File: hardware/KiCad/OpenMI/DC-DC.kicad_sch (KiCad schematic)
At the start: 37 parts, among them Q4 GAN7R0-150LBEZ, Q5 GAN7R0-150LBEZ, U3 1EDN7550B, U4 1EDN7550B

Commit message: feat: adds first considerations about rectifier
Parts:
- removed C8, C9: C, symbol Device:C
- added D6, D7: D, symbol Device:D
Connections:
- net GND2: now also D6.2 (A)
- net T_{OUT2}: now also D6.1 (K), D7.2 (A)
- net V_{BUS}: now also D7.1 (K)
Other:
- note added: "Infineon, IDD03SG60CXTMA2, 0,815€@2500pcs, Vf=2.1V, Ir=230nA, If=3A, Vrrm=600V, package=TO-252-3"
- note added: "Possible SiC diodes:"
- note added: "Rectifier"
- note added: "ST, STPSC10065G2-TR, 1.78@2000pcs, Vf=1.3V, Ir=7uA, If=10A, Vrrm=650V, package=D2PAK-3"
- note added: "TODO: Capacitor size?"
- note added: "TODO: Which SiC diode?"
- note removed: "P_{OUT} = 400W η = 0.97 P_{IN} = P_{OUT} / η = 413W V_{MPPT_{min}} = 27V V_{MPPT_{max}} = 45V I_{in_{max}} = P_{IN} / V_{MPPT_{min}} = 15.3A I_{in_max_sc} = 15A or 20A"
- moved on the sheet: C10, D3, D4

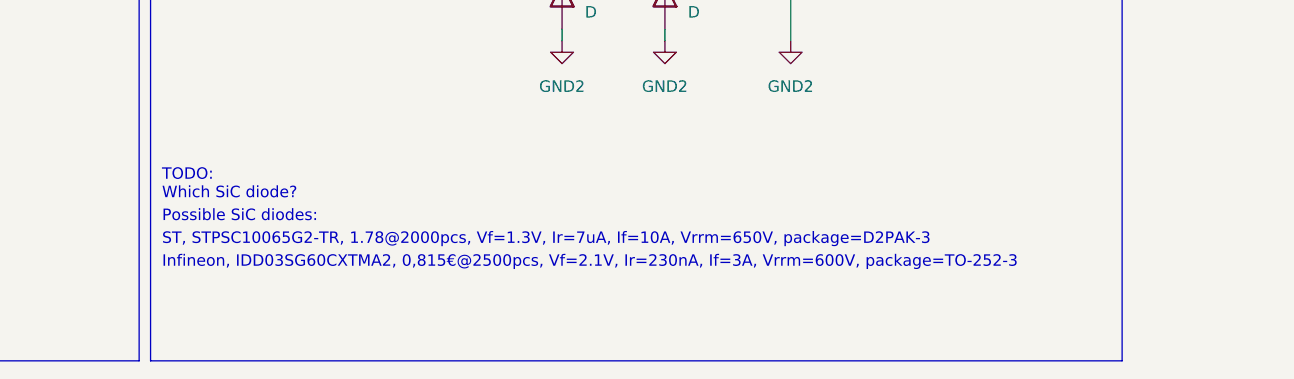
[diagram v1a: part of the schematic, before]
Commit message: docs(hw): adds new suggestion for SiC diode
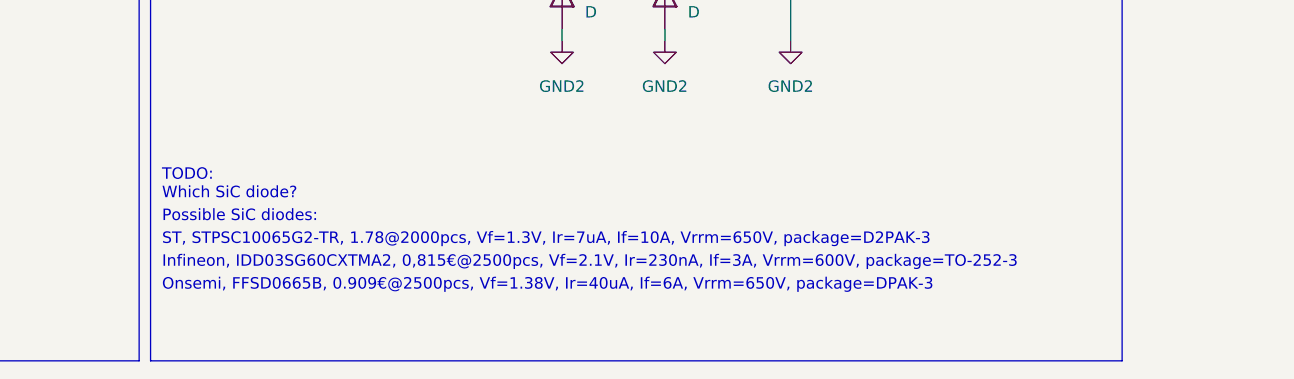
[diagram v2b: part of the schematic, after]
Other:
- note added: "Onsemi, FFSD0665B, 0.909€@2500pcs, Vf=1.38V, Ir=40uA, If=6A, Vrrm=650V, package=DPAK-3"
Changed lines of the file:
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@@
     (effects (font (size 1.27 1.27)) (justify left bottom))
+  )
+  (text "Onsemi, FFSD0665B, 0.909€@2500pcs, Vf=1.38V, Ir=40uA, If=6A, Vrrm=650V, package=DPAK-3"
+    (at 261.62 228.6 0)
+    (effects (font (size 1.27 1.27)) (justify left bottom) (href "https://www.mouser.de/ProductDetail/onsemi/FFSD0665B?qs=d0WKAl%252BL4KaoIw7wINi9oQ%3D%3D"))
   )
   (text "TODO:\nWhat turning ratio would you choose from this?\n"

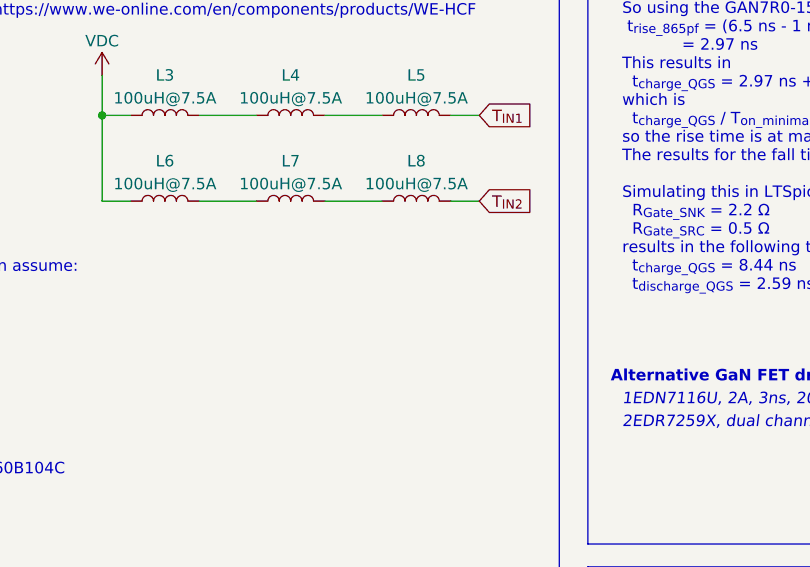
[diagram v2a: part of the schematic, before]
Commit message: docs(hw): adds todo to consider skin effect for current limit of inductor
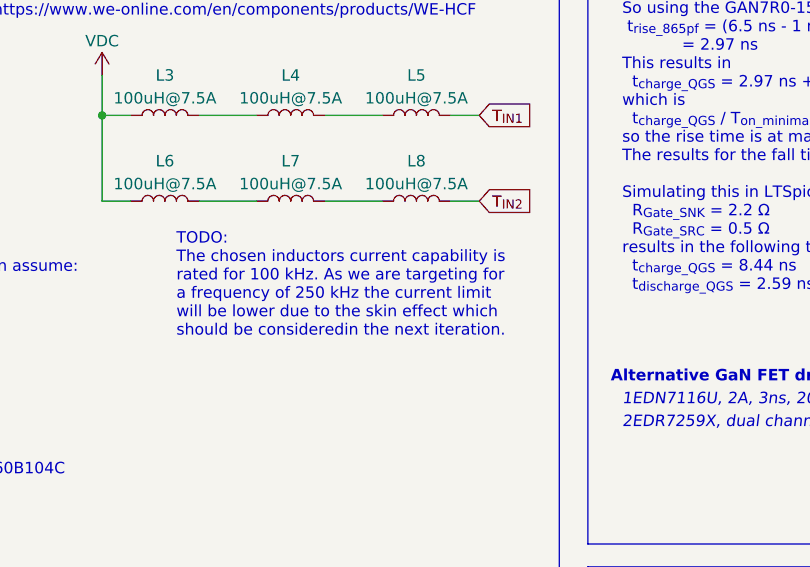
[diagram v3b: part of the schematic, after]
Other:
- note added: "TODO: The chosen inductors current capability is rated for 100 kHz. As we are targeting for a frequency of 250 kHz the current limit will be lower due to the skin effect which should be consideredin the next iteration."
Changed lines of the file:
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@@
     (effects (font (size 1.27 1.27) italic) (justify left bottom) (href "https://www.infineon.com/dgdl/Infineon-EiceDRIVER_1EDN_TDI_1EDNx550-ApplicationNotes-v02_00-EN.pdf?fileId=5546d462636cc8fb016387e66c73160f"))
+  )
+  (text "TODO:\nThe chosen inductors current capability is\nrated for 100 kHz. As we are targeting for\na frequency of 250 kHz the current limit\nwill be lower due to the skin effect which\nshould be consideredin the next iteration."
+    (at 92.71 138.43 0)
+    (effects (font (size 1.27 1.27) (color 255 0 0 1)) (justify left bottom))
   )
   (text "Infineon, IDD03SG60CXTMA2, 0,815€@2500pcs, Vf=2.1V, Ir=230nA, If=3A, Vrrm=600V, package=TO-252-3"

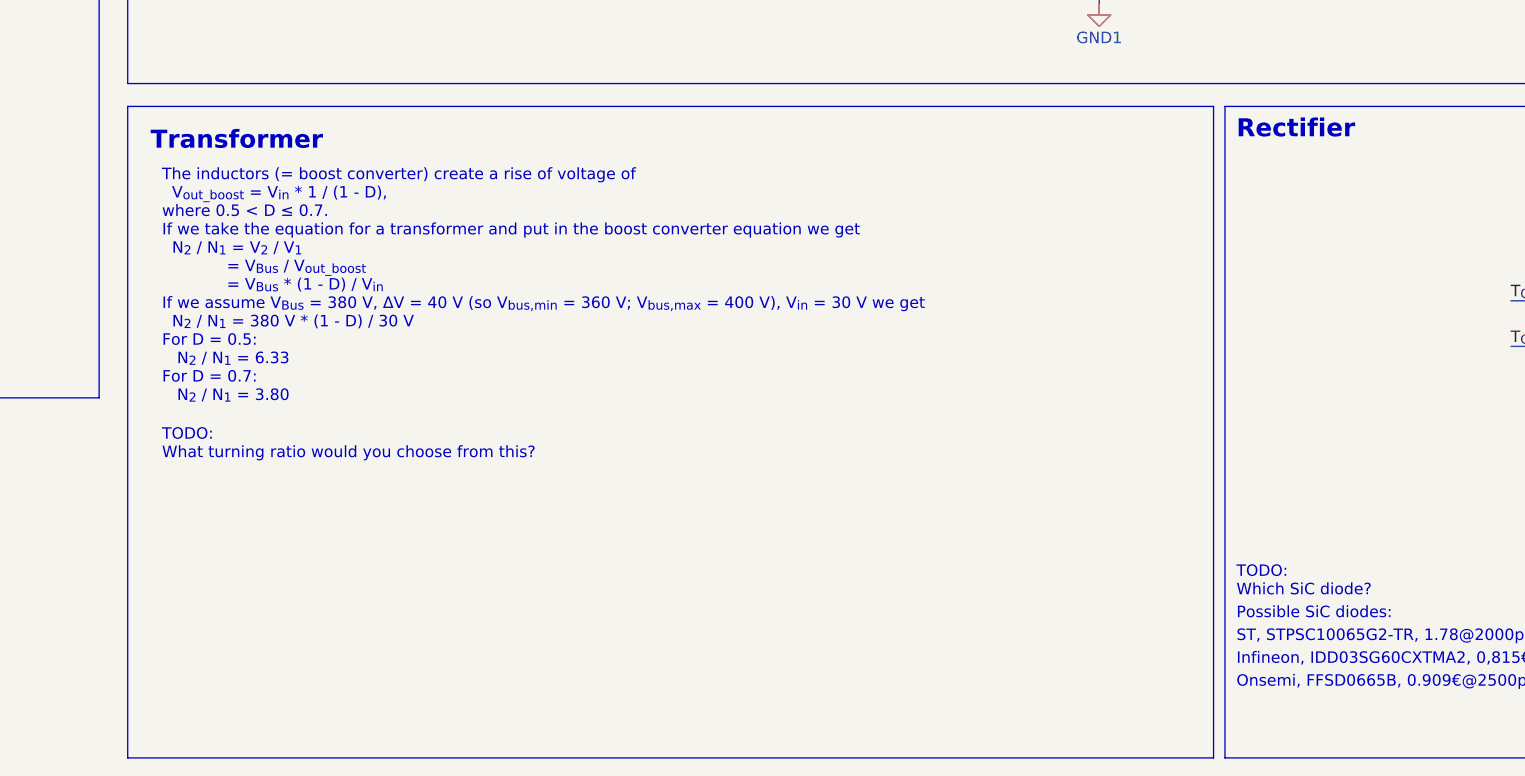
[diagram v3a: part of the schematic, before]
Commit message: docs(hw): adds more considerations for transformer design
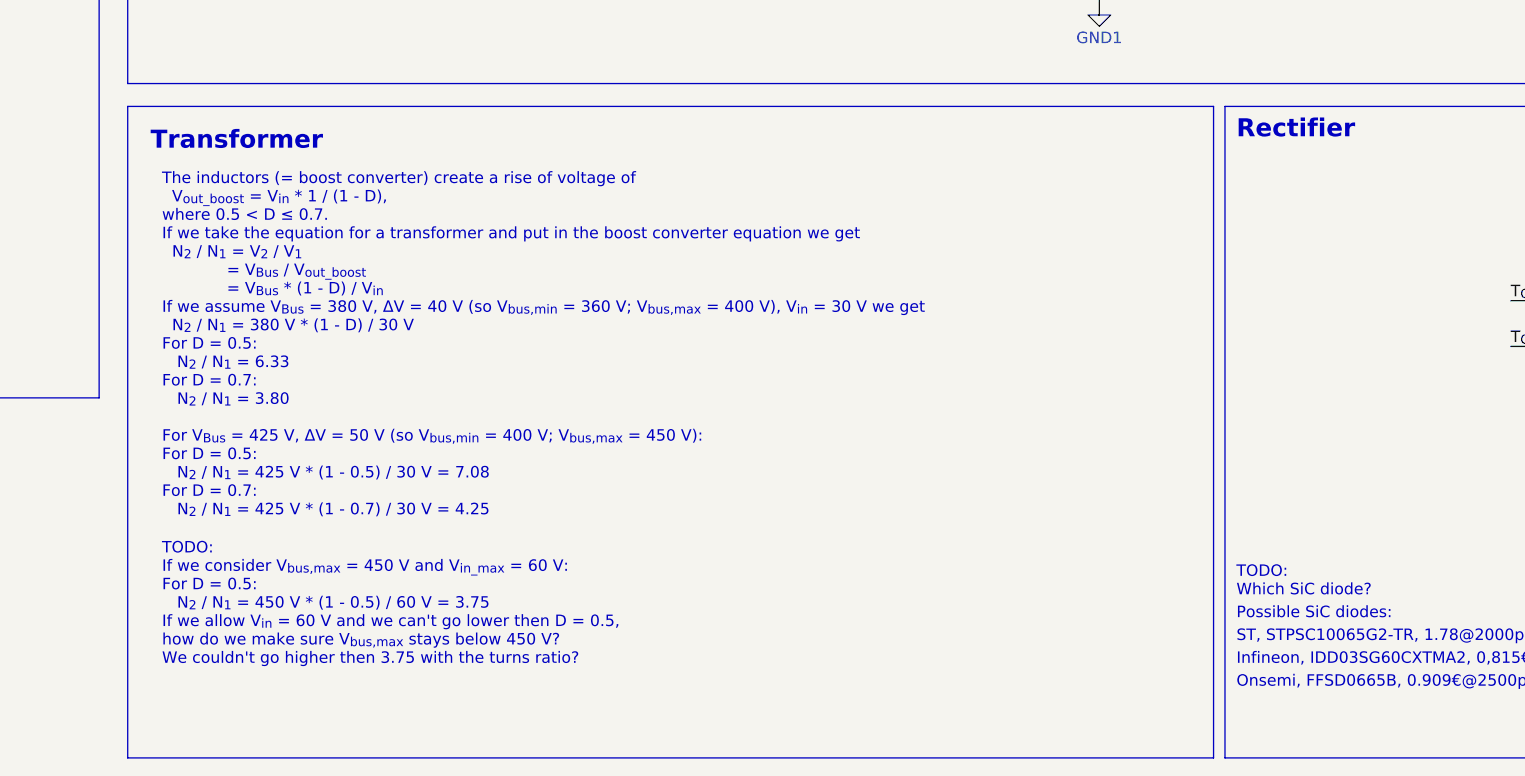
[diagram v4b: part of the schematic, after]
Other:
- note added: "TODO: If we consider V_{bus,max} = 450 V and V_{in_max} = 60 V: For D = 0.5: N_{2} / N_{1} = 450 V * (1 - 0.5) / 60 V = 3.75 If we allow V_{in} = 60 V and we can't go lower then D = 0.5, how do we make sure V_{bus,max} stays below 450 V? We couldn't go higher then 3.75 with the turns ratio?"
- note removed: "TODO: What turning ratio would you choose from this?"
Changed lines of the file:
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@@
     (effects (font (size 1.27 1.27)) (justify left bottom))
   )
-  (text "The inductors (= boost converter) create a rise of voltage of\n  V_{out_boost} = V_{in} * 1 / (1 - D),\nwhere 0.5 < D ≤ 0.7.\nIf we take the equation for a transformer and put in the boost converter equation we get\n  N_{2} / N_{1} = V_{2} / V_{1} \n             = V_{Bus} / V_{out_boost} \n             = V_{Bus} * (1 - D) / V_{in}\nIf we assume V_{Bus} = 380 V, ΔV = 40 V (so V_{bus,min} = 360 V; V_{bus,max} = 400 V), V_{in} = 30 V we get\n  N_{2} / N_{1} = 380 V * (1 - D) / 30 V\nFor D = 0.5:\n   N_{2} / N_{1} = 6.33\nFor D = 0.7:\n   N_{2} / N_{1} = 3.80"
-    (at 142.24 196.85 0)
+  (text "The inductors (= boost converter) create a rise of voltage of\n  V_{out_boost} = V_{in} * 1 / (1 - D),\nwhere 0.5 < D ≤ 0.7.\nIf we take the equation for a transformer and put in the boost converter equation we get\n  N_{2} / N_{1} = V_{2} / V_{1} \n             = V_{Bus} / V_{out_boost} \n             = V_{Bus} * (1 - D) / V_{in}\nIf we assume V_{Bus} = 380 V, ΔV = 40 V (so V_{bus,min} = 360 V; V_{bus,max} = 400 V), V_{in} = 30 V we get\n  N_{2} / N_{1} = 380 V * (1 - D) / 30 V\nFor D = 0.5:\n   N_{2} / N_{1} = 6.33\nFor D = 0.7:\n   N_{2} / N_{1} = 3.80\n\nFor V_{Bus} = 425 V, ΔV = 50 V (so V_{bus,min} = 400 V; V_{bus,max} = 450 V):\nFor D = 0.5:\n   N_{2} / N_{1} = 425 V * (1 - 0.5) / 30 V = 7.08\nFor D = 0.7:\n   N_{2} / N_{1} = 425 V * (1 - 0.7) / 30 V = 4.25"
+    (at 142.24 209.55 0)
     (effects (font (size 1.27 1.27)) (justify left bottom))
   )
@@
     (effects (font (size 1.27 1.27)) (justify left bottom) (href "https://www.mouser.de/ProductDetail/onsemi/FFSD0665B?qs=d0WKAl%252BL4KaoIw7wINi9oQ%3D%3D"))
   )
-  (text "TODO:\nWhat turning ratio would you choose from this?\n"
-    (at 142.24 203.2 0)
+  (text "TODO:\nIf we consider V_{bus,max} = 450 V and V_{in_max} = 60 V:\nFor D = 0.5:\n   N_{2} / N_{1} = 450 V * (1 - 0.5) / 60 V = 3.75\nIf we allow V_{in} = 60 V and we can't go lower then D = 0.5,\nhow do we make sure V_{bus,max} stays below 450 V?\nWe couldn't go higher then 3.75 with the turns ratio?"
+    (at 142.24 226.06 0)
     (effects (font (size 1.27 1.27) (color 255 0 0 1)) (justify left bottom))
   )

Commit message: fix(hw): changes direction of TVS diodes for GaN FET
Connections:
- net GND1: now also F1.2 (A), F2.2 (A); no longer F1.1 (K), F2.1 (K)
- net T_{IN1}: now also F2.1 (K); no longer F2.2 (A)
- net T_{IN2}: now also F1.1 (K); no longer F1.2 (A)
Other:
- moved on the sheet: F1, F2
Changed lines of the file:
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@@
     )
   )
-  (symbol (lib_id "_Diode_TVS:SMBJ100A") (at 334.01 142.24 90) (unit 1)
+  (symbol (lib_id "_Diode_TVS:SMBJ100A") (at 334.01 142.24 270) (unit 1)
     (in_bom yes) (on_board yes) (dnp no) (fields_autoplaced)
     (property "Reference" "F2" (at 336.55 141.605 90)
-      (effects (font (size 1.27 1.27)) (justify right))
+      (effects (font (size 1.27 1.27)) (justify left))
     )
     (property "Value" "SMBJ100A" (at 336.55 144.145 90)
-      (effects (font (size 1.27 1.27)) (justify right))
+      (effects (font (size 1.27 1.27)) (justify left))
     )
     (property "Footprint" "Diode_SMD:D_SMB" (at 334.01 142.24 0)
@@
     )
   )
-  (symbol (lib_id "_Diode_TVS:SMBJ100A") (at 270.51 142.24 90) (unit 1)
+  (symbol (lib_id "_Diode_TVS:SMBJ100A") (at 270.51 142.24 270) (unit 1)
     (in_bom yes) (on_board yes) (dnp no) (fields_autoplaced)
     (property "Reference" "F1" (at 273.05 141.605 90)
-      (effects (font (size 1.27 1.27)) (justify right))
+      (effects (font (size 1.27 1.27)) (justify left))
     )
     (property "Value" "SMBJ100A" (at 273.05 144.145 90)
-      (effects (font (size 1.27 1.27)) (justify right))
+      (effects (font (size 1.27 1.27)) (justify left))
     )
     (property "Footprint" "Diode_SMD:D_SMB" (at 270.51 142.24 0)
